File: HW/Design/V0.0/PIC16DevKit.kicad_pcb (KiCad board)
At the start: 4 copper layers, 68.8 x 54 mm, 105 parts, among them J1 9V-12V, J2 USB C, J3 EXP PORT, J4 SIL04, J5 QWIIC, Q1 SI2301, Q3 SI2301, Q4 2N3906, Q5 SI2302, Q6 SI2302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

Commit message: PIC16-DevKit-PCB-877 production update
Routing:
- net +3.3V: track 74.6 -> 73.8 mm
- added copper zone on B.Cu, net +3.3V
- added copper zone on F.Cu, net +3.3V
- added copper zone on In1.Cu, net +3.3V
- added copper zone on In2.Cu, net +3.3V

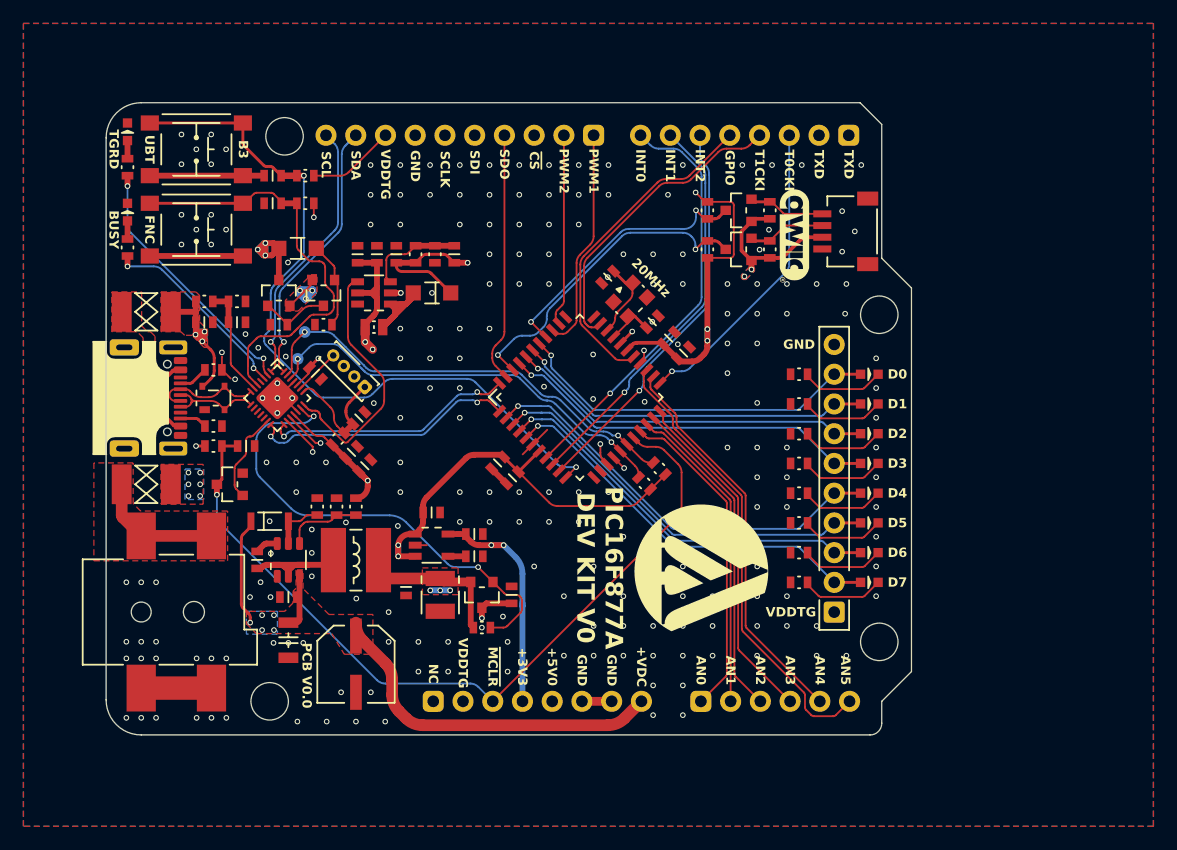
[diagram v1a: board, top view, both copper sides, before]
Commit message: PIC16-DevKit-PCB-877 V0.1 - QWIIC ESD protection, disable VPP, detect VBUS, measure VPP, VDDTG
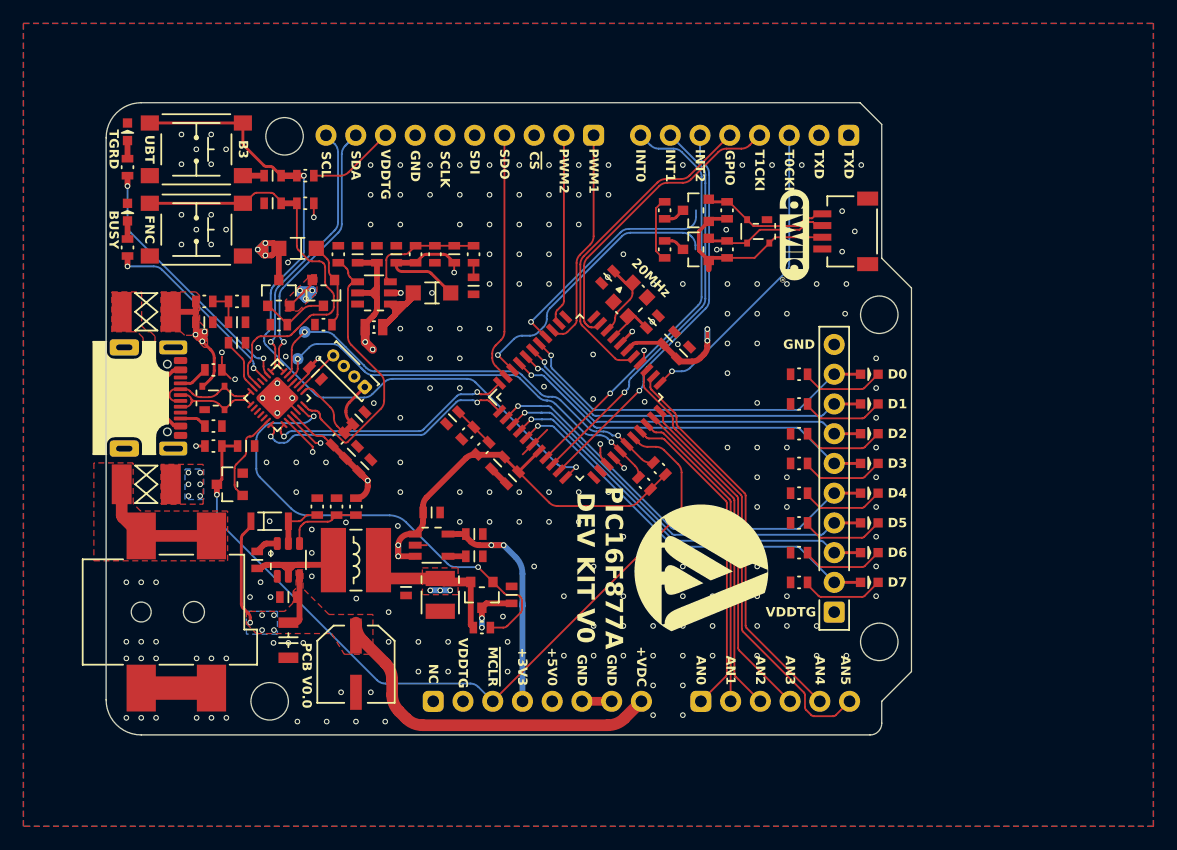
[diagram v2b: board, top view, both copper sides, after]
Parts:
- added C23: 470nF, SAMPI:CAP0603, F.Cu at (71.9, 63.5)
- added C40: 100nF, SAMPI:CAP0603, F.Cu at (90.3, 70.0)
- added C41: 100nF, SAMPI:CAP0603, F.Cu at (92.1, 58.7)
- added D5: TVS 5V, SAMPI:SOT143B_NEXT, F.Cu at (116.4, 54.0)
- added R31: 100K, SAMPI:RES0603, F.Cu at (80.5, 56.0)
- added R34: 47K, 1%, SAMPI:RES0603, F.Cu at (92.9, 72.6)
- added R35: 5.1K, 1%, SAMPI:RES0603, F.Cu at (91.6, 71.3)
- added R36: 10K, 1%, SAMPI:RES0603, F.Cu at (92.1, 56.0)
- R32: value 10K, 1% -> 5.1K, 1%
- R33: value 10K, 1% -> 47K, 1%
- moved Q6 3.65 mm to (111.0, 52.2)
- moved Q7 3.65 mm to (111.0, 55.6)
- moved R21 3.65 mm to (108.4, 55.6)
- moved R22 3.65 mm to (108.4, 52.2)
- moved R28 3.65 mm to (113.7, 52.2)
- moved R30 3.65 mm to (113.7, 55.6)
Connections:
- C39 pad 1: /POWER/VBUS_SEN -> /POWER/VBUS_DIV
- R32 pad 1: /POWER/VBUS_SEN -> /POWER/VBUS_DIV
- R33 pad 2: /POWER/VBUS_SEN -> /POWER/VBUS_DIV
- U5 pad 10: unconnected-(U5-PD0/ACINN/AIN7-Pad10) -> /POWER/VPP_DIV
- U5 pad 11: unconnected-(U5-PD1/AIN8-Pad11) -> /POWER/VDDTG_DIV
- U5 pad 6: /POWER/VBUS_SEN -> Net-(U5-VUSB)
- U5 pad 9: unconnected-(U5-PC3/ACINP/AIN6-Pad9) -> /POWER/VBUS_DIV
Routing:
- net +VDDTG: track 209.2 -> 192.3 mm, vias 7 -> 6
- net GND: track 40.0 -> 24.1 mm, vias 224 -> 219
- net /POWER/VBUS_SEN: track 9.63 -> 0.00 mm
- net Net-(U5-VUSB): track 0.00 -> 4.74 mm
- net Net-(D5-CH1): track 6.52 -> 11.1 mm
- net Net-(D5-CH2): track 6.66 -> 10.8 mm
- net +3.3V: track 73.8 -> 77.5 mm, vias 4 -> 2
- net /POWER/VDDTG_DIV: track 0.00 -> 3.68 mm
- net /POWER/VBUS_DIV: track 0.00 -> 3.12 mm
- net /POWER/VPP_EN: track 21.9 -> 24.4 mm
- net Net-(U3-FB): track 8.34 -> 9.94 mm
- net /PROGRAMMER/SDA: track 86.2 -> 84.9 mm, vias 3 -> 2
- net /POWER/VPP_DIV: track 0.00 -> 1.24 mm
- net /PROGRAMMER/SCL: track 75.8 -> 74.7 mm, vias 3 -> 2
- net /PROGRAMMER/~{BT_FNC}: track 37.2 -> 36.6 mm
- removed copper zone on B.Cu, net +3.3V
- removed copper zone on F.Cu, net +3.3V
- removed copper zone on In1.Cu, net +3.3V
- removed copper zone on In2.Cu, net +3.3V
